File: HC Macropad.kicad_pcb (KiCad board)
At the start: 2 copper layers, 168.2 x 34 mm, 63 parts, among them J1 USB_C_Receptacle_USB2.0_16P, J2 Conn_01x02_Socket, J3 Conn_01x04_Socket, SW1 SW_Push, U1 RP2040, U2 W25Q128JVPIQ, U3 AP2127K-3.3, U4 USBLC6-2P6, Y1 Crystal_GND24

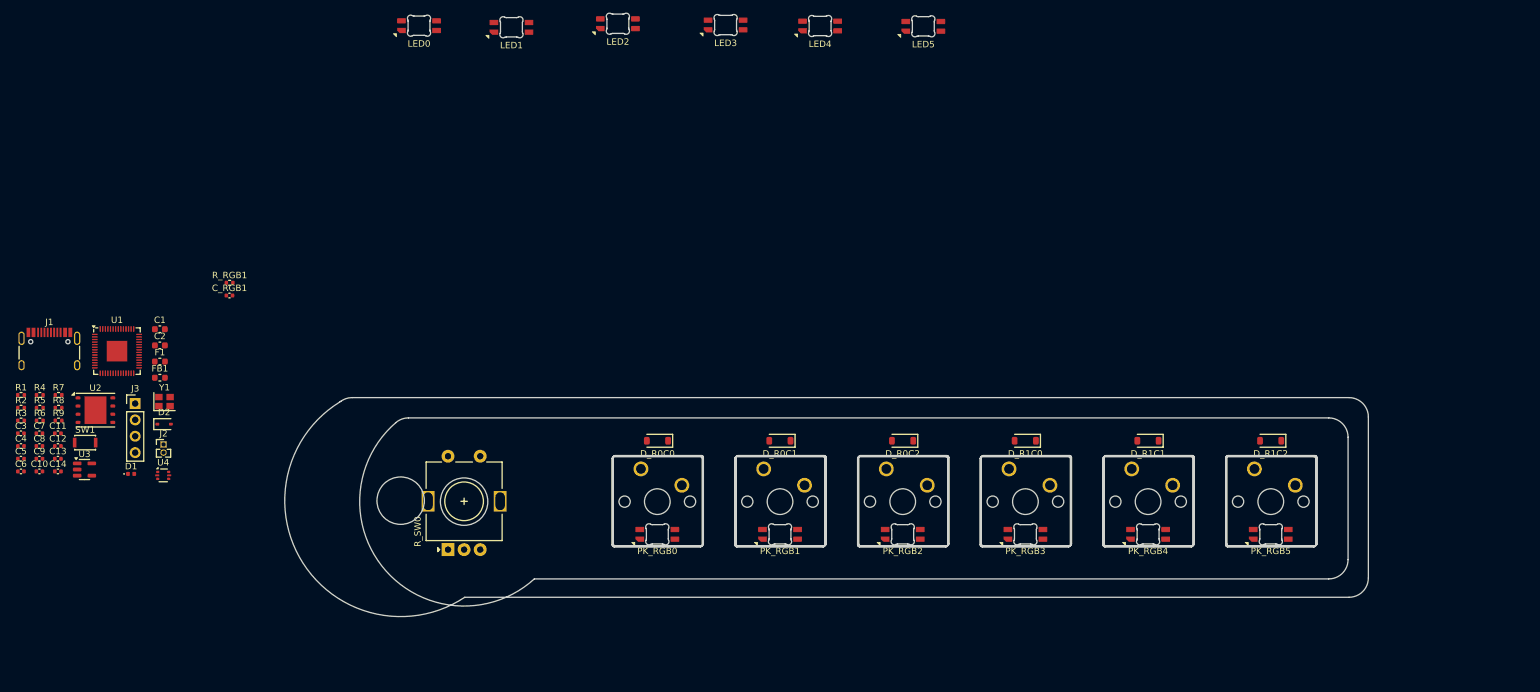
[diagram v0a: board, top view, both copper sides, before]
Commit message: Move switches, diodes, and LEDs to their final location
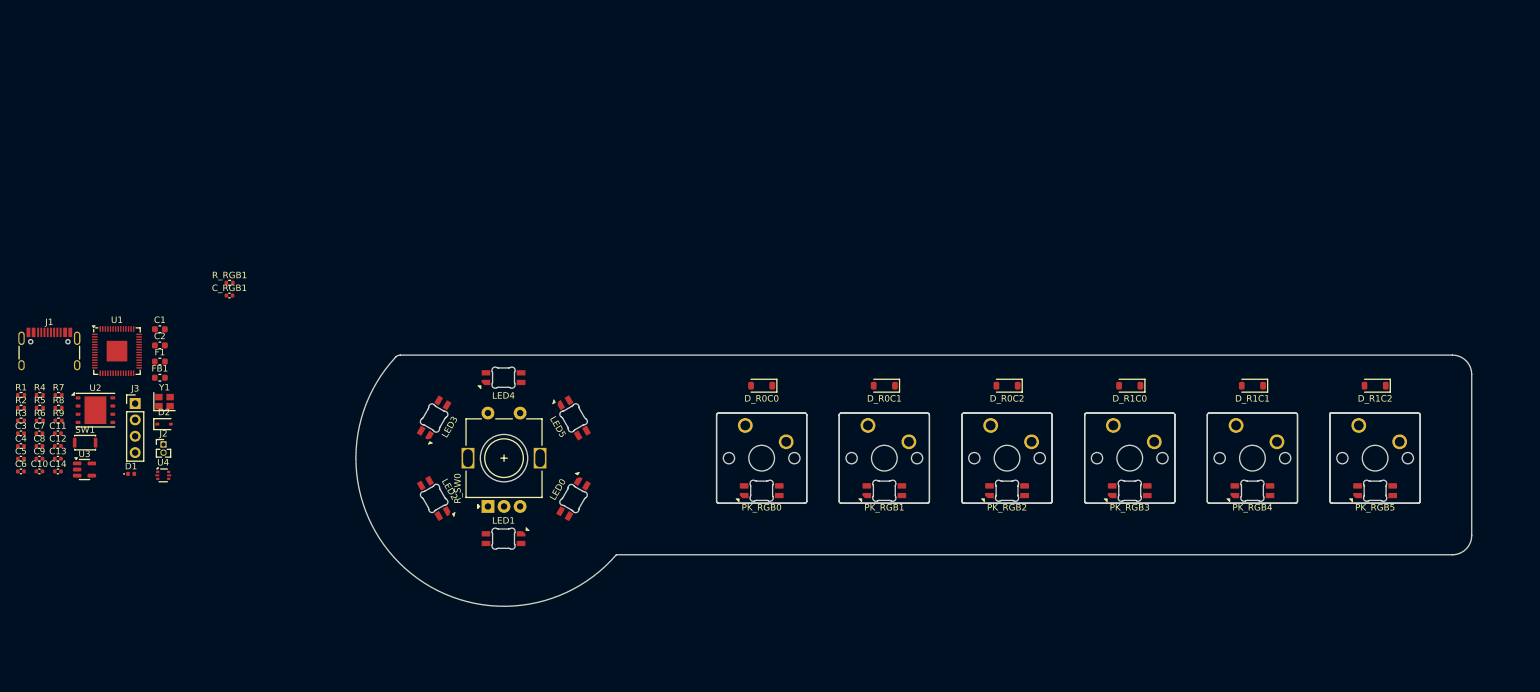
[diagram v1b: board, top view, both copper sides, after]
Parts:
- moved LED5 81.5 mm to (106.0, 86.5), turned to -60 degrees
- moved LED1 79.4 mm to (95.1, 105.2), turned to 180 degrees
- moved LED2 79.0 mm to (84.3, 99.0), turned to 120 degrees
- moved LED0 77.2 mm to (105.9, 99.0), turned to -120 degrees
- moved LED3 76.0 mm to (84.3, 86.5), turned to 60 degrees
- moved LED4 73.5 mm to (95.1, 80.2)
- moved D_R1C0 18.3 mm to (192.3, 81.5)
- moved D_R0C1 18.3 mm to (154.2, 81.5)
- moved D_R0C2 18.3 mm to (173.2, 81.5)
- moved D_R1C1 18.3 mm to (211.3, 81.5)
- moved D_R1C2 18.3 mm to (230.4, 81.5)
- moved D_R0C0 18.3 mm to (135.2, 81.5)
- moved PK_RGB3 17.6 mm to (192.3, 97.8)
- moved PK_RGB5 17.6 mm to (230.4, 97.8)
- moved PK_RGB0 17.6 mm to (135.2, 97.8)
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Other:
- board size 168.2 x 34 mm -> 173.2 x 39 mm

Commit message: 90% of routing done
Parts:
- added J4: Conn_01x04_Socket, Connector_PinHeader_2.54mm:PinHeader_1x04_P2.54mm_Vertical, F.Cu at (123.5, 74.1)
- added J5: Conn_01x04_Socket, Connector_PinHeader_2.54mm:PinHeader_1x04_P2.54mm_Vertical, F.Cu at (123.5, 79.3)
- moved R1 109.1 mm to (127.0, 105.1), turned to 90 degrees
- moved C5 103.8 mm to (123.9, 89.8), turned to 90 degrees
- moved R2 103.3 mm to (121.8, 103.4)
- moved C6 102.8 mm to (122.9, 89.8), turned to 90 degrees
- moved R4 100.3 mm to (122.3, 68.2), turned to -90 degrees
- moved C8 99.3 mm to (121.8, 101.4)
- moved C4 98.3 mm to (117.5, 104.3), turned to 180 degrees
- moved C13 98.2 mm to (124.0, 96.9), turned to -90 degrees
- moved C11 98.2 mm to (124.0, 92.3), turned to 90 degrees
- moved R6 97.1 mm to (120.2, 89.6), turned to -90 degrees
- moved C3 96.6 mm to (115.5, 104.3)
- moved J1 96.5 mm to (119.8, 61.8), turned to 180 degrees
- moved C14 96.2 mm to (121.8, 102.4)
- moved C7 96.1 mm to (119.2, 89.6), turned to 90 degrees
- moved R5 95.7 mm to (117.3, 68.2), turned to -90 degrees
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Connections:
- U1 pad 11: M_COL2 -> ENC_SW0
- U1 pad 12: ENC_PIN0 -> ENC_SW1
- U1 pad 14: ENC_SW0 -> ENC_PIN0
- U1 pad 15: ENC_SW1 -> unconnected-(U1-GPIO12-Pad15)
- U1 pad 36: unconnected-(U1-GPIO24-Pad36) -> M_ROW1
- U1 pad 37: unconnected-(U1-GPIO25-Pad37) -> M_ROW0
- U1 pad 38: unconnected-(U1-GPIO26_ADC0-Pad38) -> M_COL0
- U1 pad 39: unconnected-(U1-GPIO27_ADC1-Pad39) -> M_COL1
- U1 pad 40: unconnected-(U1-GPIO28_ADC2-Pad40) -> M_COL2
- U1 pad 6: M_ROW0 -> unconnected-(U1-GPIO4-Pad6)
- U1 pad 7: M_ROW1 -> unconnected-(U1-GPIO5-Pad7)
- U1 pad 8: M_COL0 -> unconnected-(U1-GPIO6-Pad8)
- U1 pad 9: M_COL1 -> unconnected-(U1-GPIO7-Pad9)
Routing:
- net +5V: track 0.00 -> 308.4 mm, vias 0 -> 12
- net M_COL2: track 0.00 -> 126.7 mm, vias 0 -> 2
- net M_ROW1: track 0.00 -> 115.6 mm
- net M_COL1: track 0.00 -> 106.7 mm, vias 0 -> 2
- net M_COL0: track 0.00 -> 86.7 mm, vias 0 -> 2
- net +3V3: track 0.00 -> 75.2 mm, vias 0 -> 4
- net M_ROW0: track 0.00 -> 58.6 mm
- net GND: track 0.00 -> 46.8 mm, vias 0 -> 14
- net /MCU/SWCLK: track 0.00 -> 42.6 mm, vias 0 -> 1
- net /MCU/SWD: track 0.00 -> 40.9 mm, vias 0 -> 1
- net /MCU/D+: track 0.00 -> 31.0 mm, vias 0 -> 2
- net /MCU/D-: track 0.00 -> 30.8 mm, vias 0 -> 2
- net ENC_SW1: track 0.00 -> 29.1 mm, vias 0 -> 1
- net ENC_PIN0: track 0.00 -> 27.5 mm, vias 0 -> 1
- net ENC_SW0: track 0.00 -> 23.7 mm, vias 0 -> 1
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- added copper zone on B.Cu, net GND
- added copper zone on F.Cu, net GND
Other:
- board size 173.2 x 39 mm -> 173.2 x 57 mm

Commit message: Finished routing
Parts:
- moved C_RGB1 3.52 mm to (113.8, 92.3), turned to 90 degrees
- moved C10 0.68 mm to (114.0, 84.0)
- moved R9 0.68 mm to (112.1, 84.4)
- moved U2 0.68 mm to (114.3, 87.8)
- moved C13 0.55 mm to (124.0, 96.3)
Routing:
- net PK_RGB: track 0.00 -> 35.5 mm, vias 0 -> 2
- net /MCU/QSPI_~{CS}: track 1.44 -> 34.6 mm, vias 0 -> 2
- net +3V3: track 75.2 -> 101.7 mm, vias 4 -> 8
- net +5V: track 308.4 -> 316.2 mm
- net GND: track 46.8 -> 54.3 mm, vias 14 -> 17
- net VBUS: track 7.40 -> 10.2 mm
- net ENC_SW1: track 29.1 -> 28.1 mm
- net /MCU/D-: track 30.8 -> 31.8 mm
- net /MCU/QSPI_D0: track 3.65 -> 2.68 mm
- net /MCU/QSPI_D3: track 6.61 -> 5.88 mm
- net ENC_PIN0: track 27.5 -> 28.2 mm
- net ENC_PIN1: track 22.1 -> 22.8 mm
